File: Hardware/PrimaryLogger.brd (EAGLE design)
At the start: 52.1 x 77.1 mm, 91 parts, among them J1 CONN_42.54_SCREW, J2 CONN_42.54_SCREW, J3 CONN_42.54_SCREW, J4 CONN_42.54_SCREW, J5 CONN_32.54_SCREW, J9 GEMS_POWER_PLUGINPUT, Q1 DMG3404, Q2 DMG3404, U1 MCP79412SOIC, U10 PCA9617, U11 SN74AUP3G34DCU, U12 SN74LVC1G3157SC70, U2 TPL5010DDC, U3 MCP23008SSOP, U4 SHTC3DFN, U5 TCS3400, U6 TPL5010DDC, U7 MIC2005, U8 MIC2005, U9 MIC842L

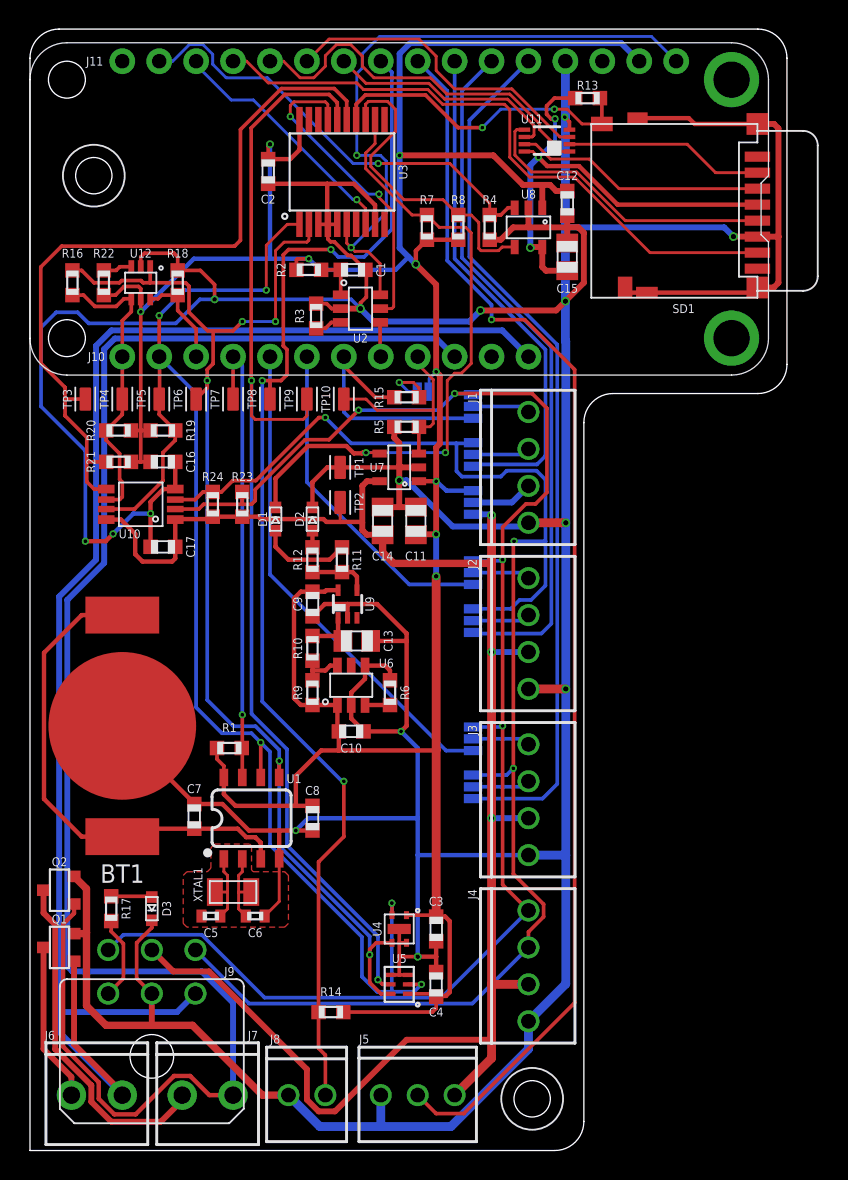
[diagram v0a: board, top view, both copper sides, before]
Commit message: v1.0 Updates
Changed pinout and added connector to support preliminary talon development
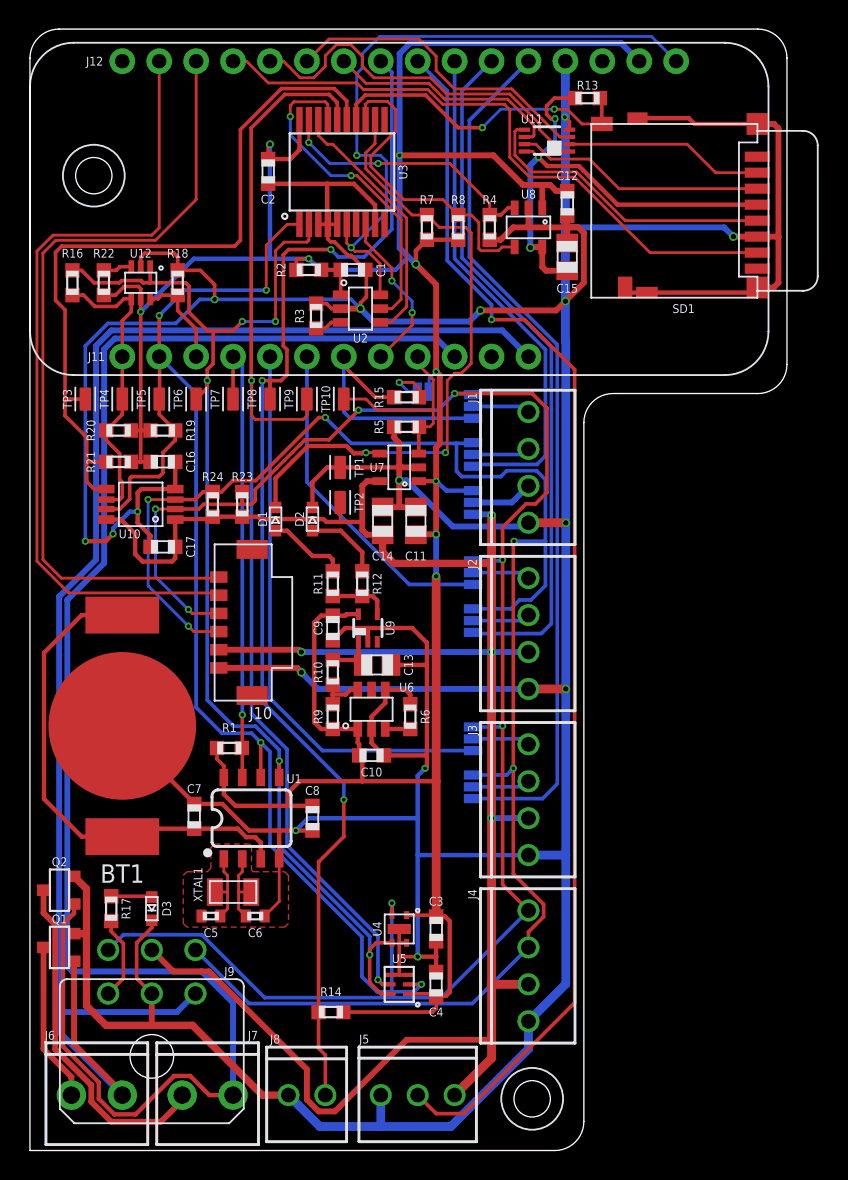
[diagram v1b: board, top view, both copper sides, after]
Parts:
- added J10: CONN_6MICROLOCK, bschulz:1X06_MICROLOCKPLUS
- MS1: value FEATHERWING_NODIM -> FEATHERWINGLAYOUT; device bschulz:FEATHERWING_DIM -> bschulz:FEATHERWING_MIN
- moved R12 3.81 mm to (22.9, 39.0)
- moved C10 2.16 mm to (23.5, 27.2)
- moved R6 2.16 mm to (26.2, 29.8)
- moved R9 2.16 mm to (20.8, 29.8)
- moved C13 2.16 mm to (23.9, 33.4)
- moved U6 2.16 mm to (23.5, 30.4)
- moved C9 2.16 mm to (20.8, 35.9)
- moved R10 2.16 mm to (20.8, 32.9)
- moved U9 2.16 mm to (23.2, 35.9)
- moved R11 1.77 mm to (20.8, 39.0)
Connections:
- new net RX: J10.1, MS1.14
- new net TX: J10.2, MS1.15
- net 3V3_EXT: now also J10.5
- net 3V3_SD_EN: now also U3.19; no longer MS1.15
- net GND: now also J10.6
- net IO_EXP_INT: now also MS1.24; no longer MS1.14
- net SCL_EXT: now also J10.3
- net SDA_EXT: now also J10.4
- net WD_HOLD: now also U3.18; no longer MS1.24
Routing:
- net TX: track 0.00 -> 55.3 mm
- net RX: track 0.00 -> 55.3 mm
- net 3V3_EXT: track 120.0 -> 138.8 mm, vias 3 -> 4
- net GND: track 416.0 -> 432.2 mm, vias 15 -> 16
- net WD_HOLD: track 2.37 -> 17.9 mm
- net SDA_EXT: track 105.5 -> 119.7 mm, vias 3 -> 5
- net 3V3_SD_EN: track 30.9 -> 18.5 mm, vias 1 -> 2
- net SCL_EXT: track 106.5 -> 118.0 mm, vias 4 -> 6
- net IO_EXP_INT: track 17.1 -> 11.3 mm, vias 1 -> 2
- net GPIO3D: track 34.0 -> 39.0 mm
- net N$12: track 1.14 -> 5.35 mm
- net WAKE: track 22.0 -> 23.1 mm
- net I2C_EXT_EN: track 52.6 -> 51.8 mm
- net N$11: track 6.40 -> 5.56 mm
- net SCL: track 95.5 -> 96.1 mm
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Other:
- board text added: "J12"
- board text added: "Project Hyena v1.0A Bobby Schulz UMN/GEMS"
- board text removed: "J10"
- board text removed: "Project Hyena v0.4A Bobby Schulz UMN/GEMS"
